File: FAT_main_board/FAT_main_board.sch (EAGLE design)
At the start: 4 parts, among them IC1 LM18200T, IC2 LM18200T, IC3 LM18200T

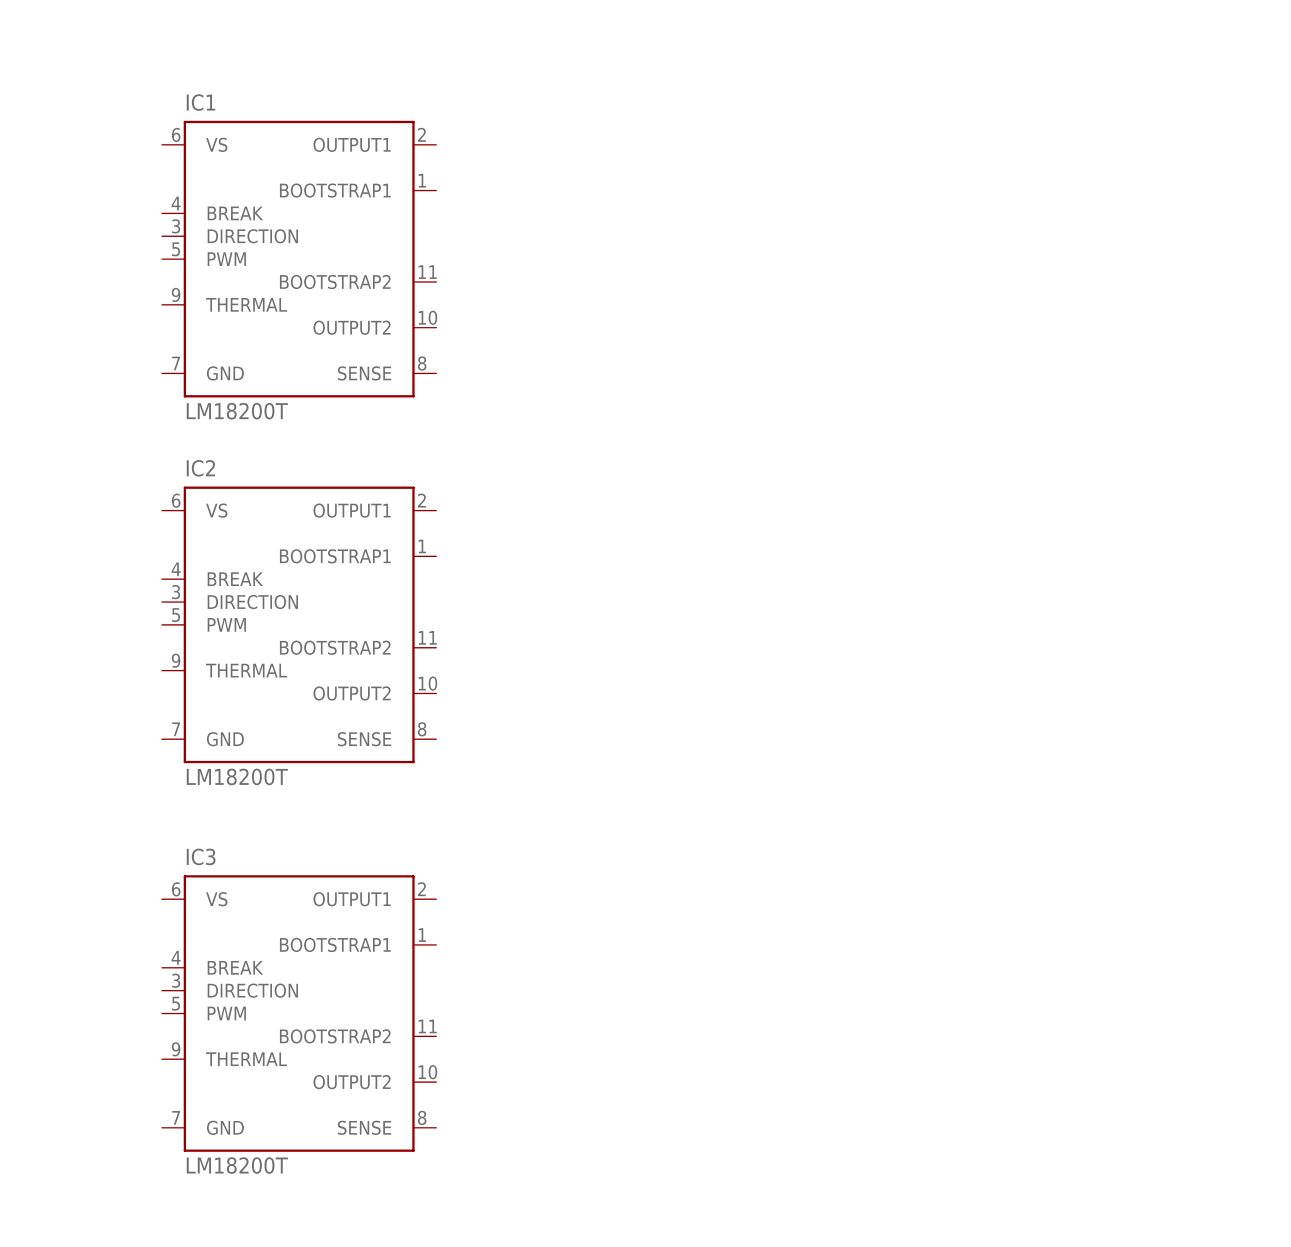
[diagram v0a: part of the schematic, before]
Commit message: [FAT board] Adds necessary components for H-bridges.
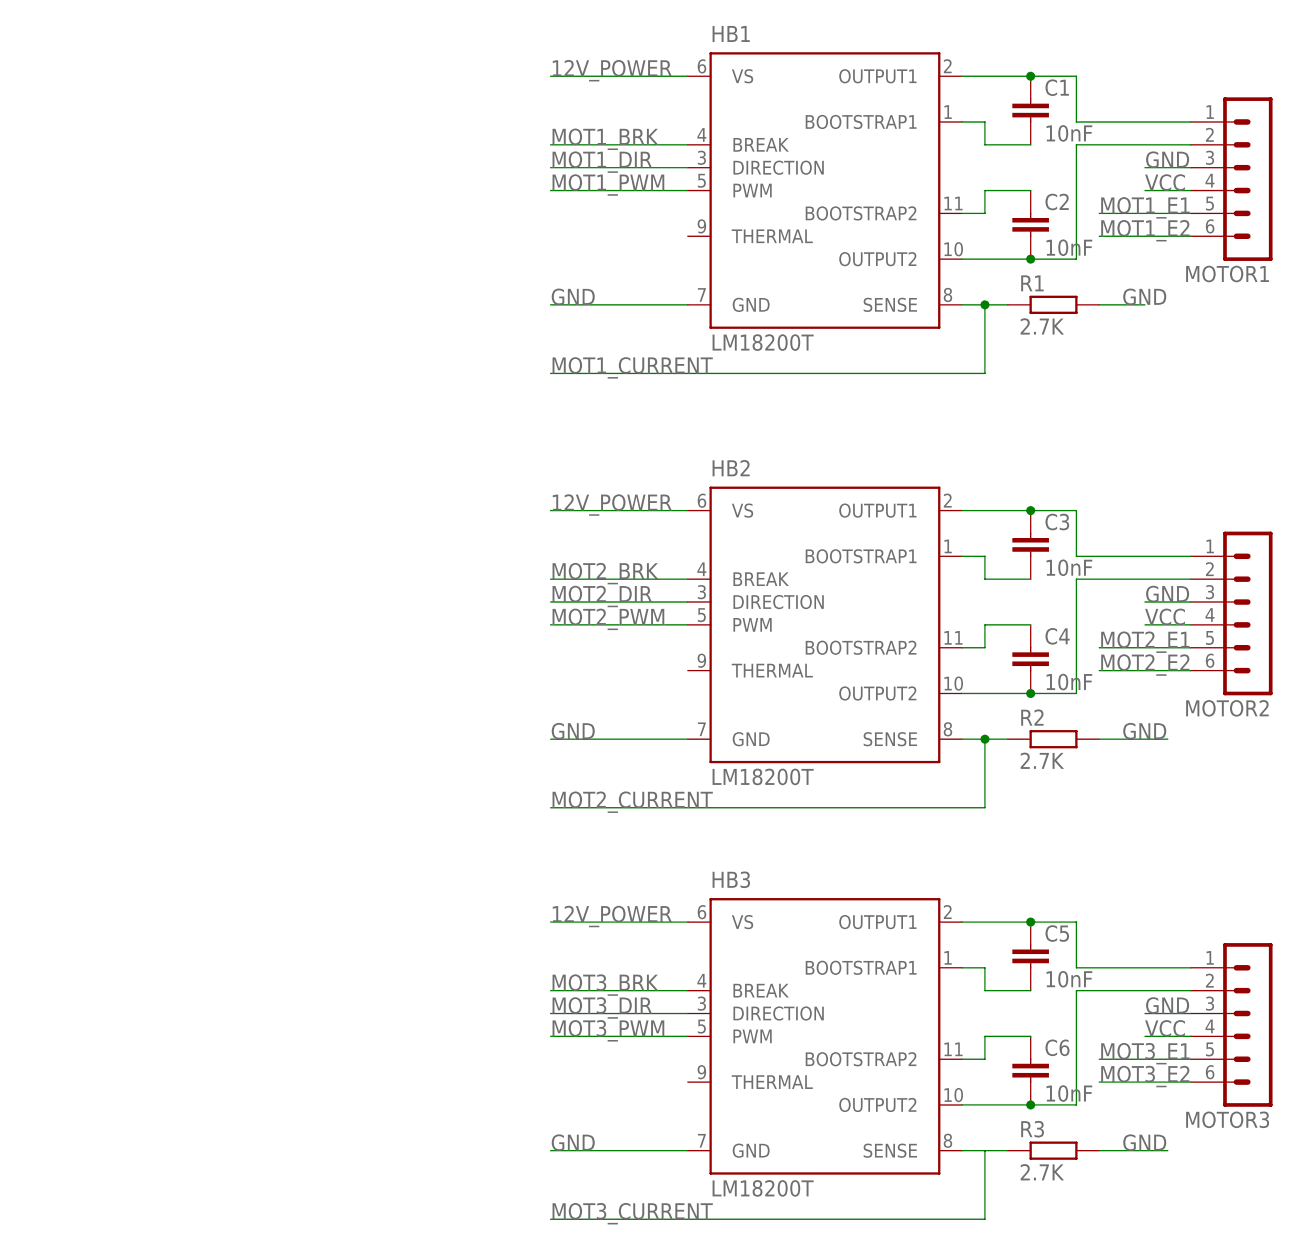
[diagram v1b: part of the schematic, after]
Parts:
- removed IC1, IC2, IC3: LM18200T, national-semiconductor:LM18200T
- added C1, C2, C3, C4, C5, C6: 10nF, resistor:C-EU050-035X075
- added HB1, HB2, HB3: LM18200T, national-semiconductor:LM18200T
- added MOTOR1, MOTOR2, MOTOR3: (no value), con-lstb:MA06-1
- added R1, R2, R3: 2.7K, resistor:R-EU_0204/7
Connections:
- new net 12V_POWER: HB1.VS, HB2.VS, HB3.VS
- new net GND: HB1.GND, HB2.GND, HB3.GND, MOTOR1.3, MOTOR2.3, MOTOR3.3, R1.2, R2.2, R3.2
- new net MOT1_BRK: HB1.BREAK
- new net MOT1_CURRENT: HB1.SENSE, R1.1
- new net MOT1_DIR: HB1.DIRECTION
- new net MOT1_E1: MOTOR1.5
- new net MOT1_E2: MOTOR1.6
- new net MOT1_PWM: HB1.PWM
- new net MOT2_BRK: HB2.BREAK
- new net MOT2_CURRENT: HB2.SENSE, R2.1
- new net MOT2_DIR: HB2.DIRECTION
- new net MOT2_E1: MOTOR2.5
- new net MOT2_E2: MOTOR2.6
- new net MOT2_PWM: HB2.PWM
- new net MOT3_BRK: HB3.BREAK
- new net MOT3_CURRENT: HB3.SENSE, R3.1
- new net MOT3_DIR: HB3.DIRECTION
- new net MOT3_E1: MOTOR3.5
- new net MOT3_E2: MOTOR3.6
- new net MOT3_PWM: HB3.PWM
- new net N$1: C1.1, HB1.OUTPUT1, MOTOR1.1
- new net N$14: C5.1, HB3.OUTPUT1, MOTOR3.1
- new net N$15: C5.2, HB3.BOOTSTRAP1
- new net N$16: C6.1, HB3.BOOTSTRAP2
- new net N$17: C6.2, HB3.OUTPUT2, MOTOR3.2
- new net N$2: C2.2, HB1.OUTPUT2, MOTOR1.2
- new net N$3: C1.2, HB1.BOOTSTRAP1
- new net N$4: C2.1, HB1.BOOTSTRAP2
- new net N$5: C3.1, HB2.OUTPUT1, MOTOR2.1
- new net N$6: C3.2, HB2.BOOTSTRAP1
- new net N$7: C4.1, HB2.BOOTSTRAP2
- new net N$8: C4.2, HB2.OUTPUT2, MOTOR2.2
- new net VCC: MOTOR1.4, MOTOR2.4, MOTOR3.4

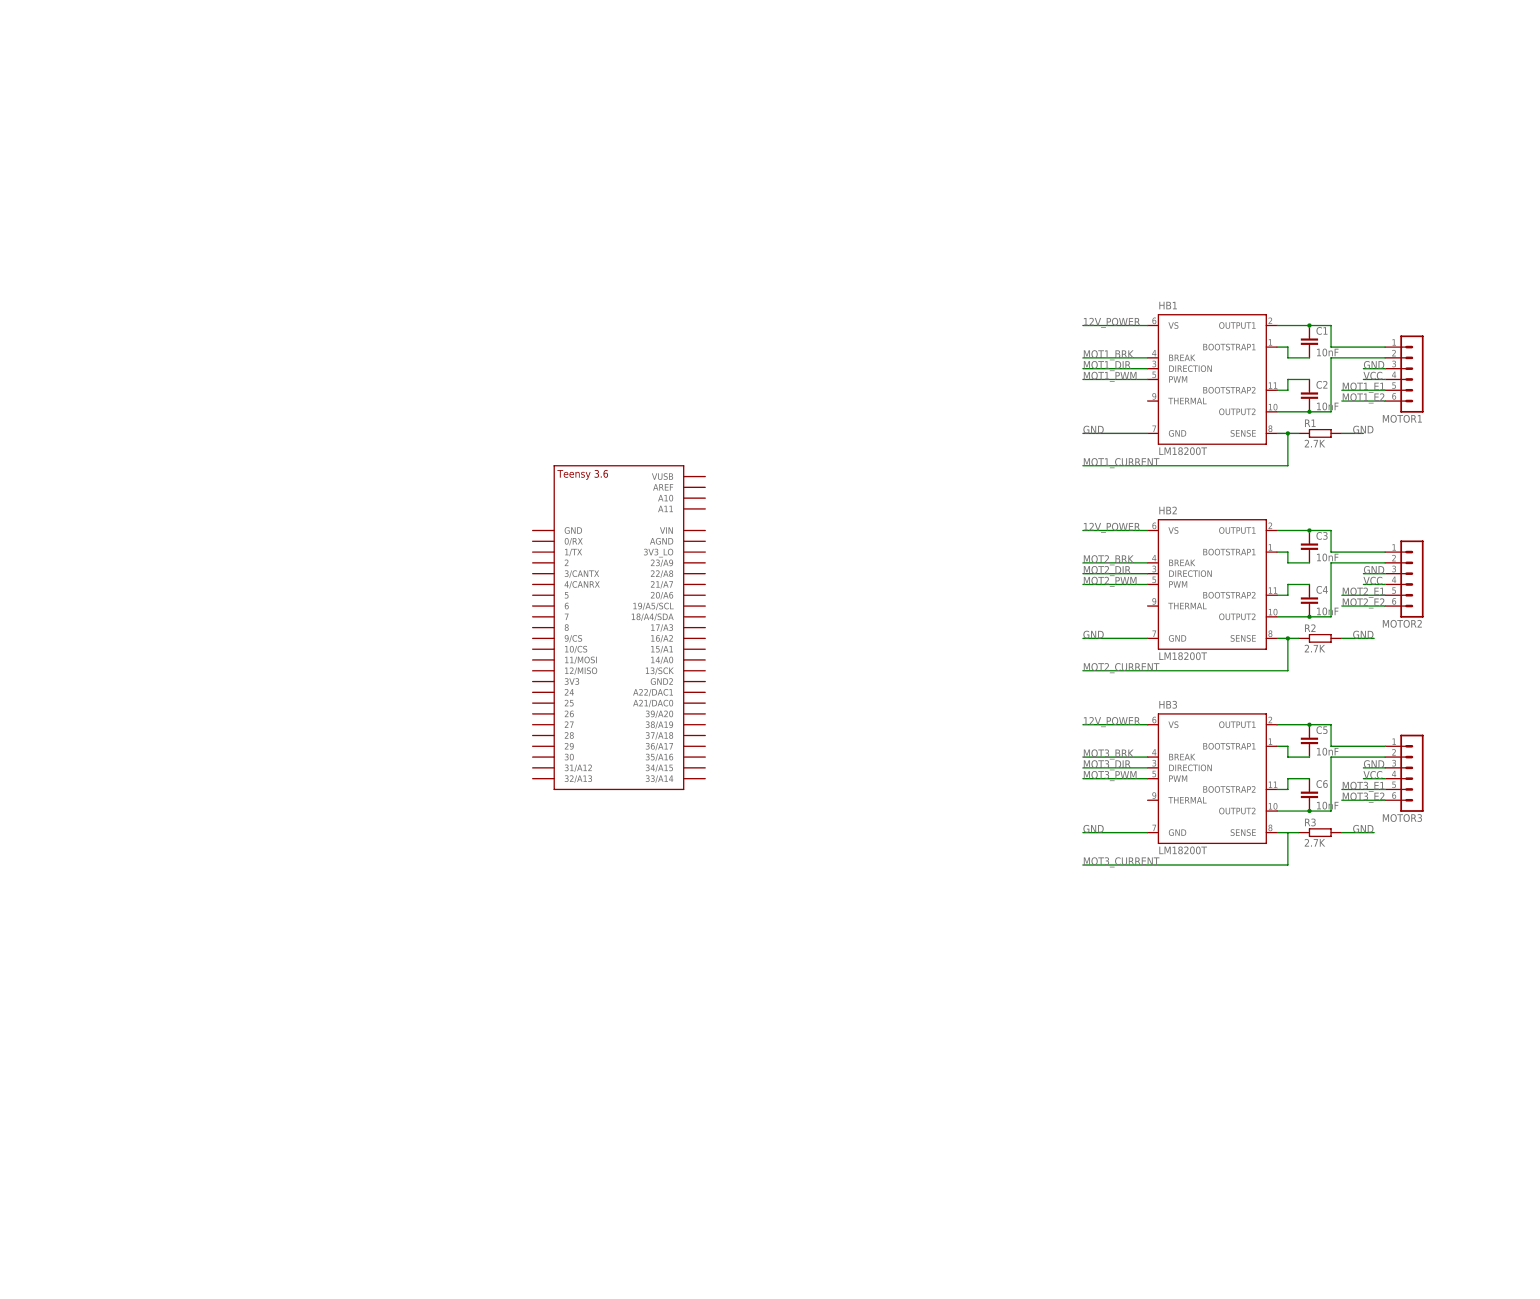
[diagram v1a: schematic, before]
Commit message: [FAT board] Connect motors to teensy and add dynamixel control.
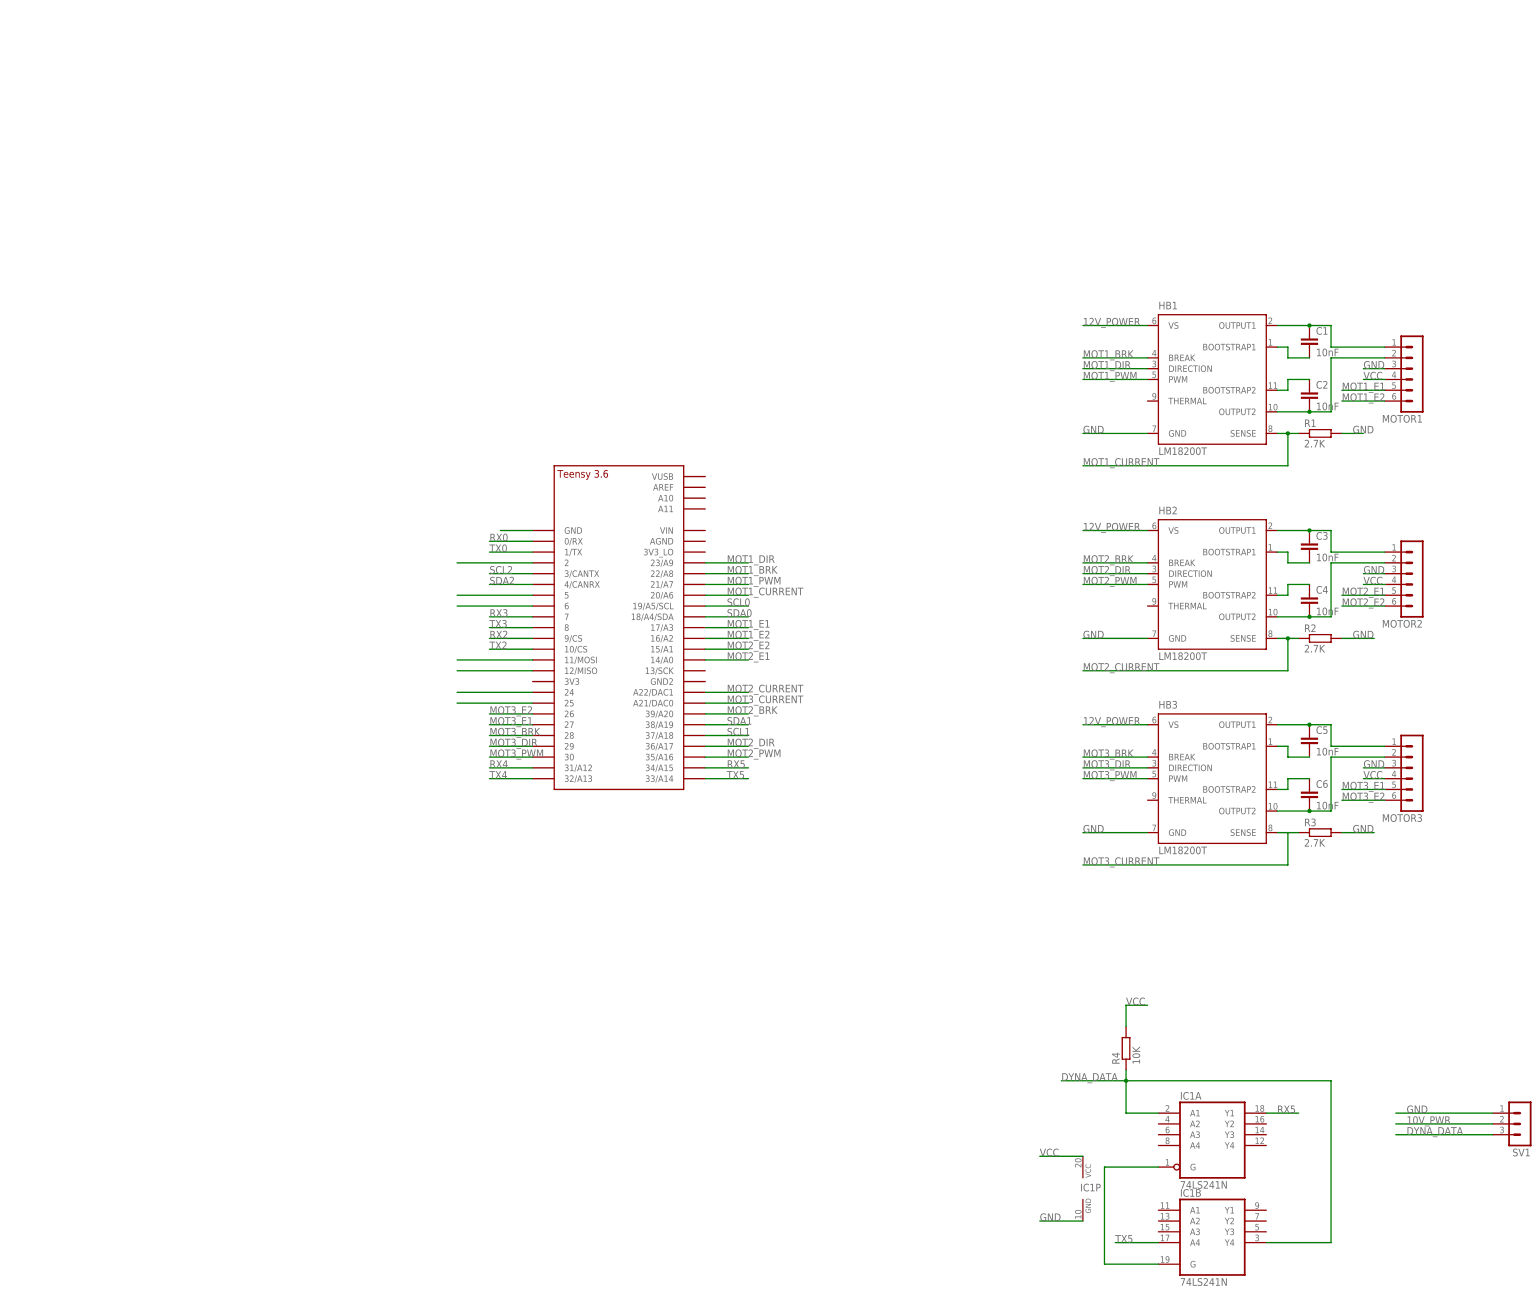
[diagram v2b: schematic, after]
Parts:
- added IC1: 74LS241N, 74xx-eu:74LS241N
- added R4: 10K, resistor:R-EU_0204/7
- added SV1: (no value), con-lstb:MA03-1
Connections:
- new net 10V_PWR: SV1.2
- new net DYNA_DATA: IC1A.A1, IC1B.Y4, R4.1, SV1.3
- new net N$10: U$1.6
- new net N$11: U$1.11/MOSI
- new net N$12: U$1.12/MISO
- new net N$13: U$1.GND
- new net N$18: U$1.2
- new net N$21: IC1A.G, IC1B.G
- new net N$40: U$1.25
- new net N$41: U$1.24
- new net N$9: U$1.5
- new net RX0: U$1.0/RX
- new net RX2: U$1.9/CS
- new net RX3: U$1.7
- new net RX4: U$1.31/A12
- new net RX5: IC1A.Y1, U$1.34/A15
- new net SCL0: U$1.19/A5/SCL
- new net SCL1: U$1.37/A18
- new net SCL2: U$1.3/CANTX
- new net SDA0: U$1.18/A4/SDA
- new net SDA1: U$1.38/A19
- new net SDA2: U$1.4/CANRX
- new net TX0: U$1.1/TX
- new net TX2: U$1.10/CS
- new net TX3: U$1.8
- new net TX4: U$1.32/A13
- new net TX5: IC1B.A4, U$1.33/A14
- net GND: now also IC1P.GND, SV1.1
- net MOT1_BRK: now also U$1.22/A8
- net MOT1_CURRENT: now also U$1.20/A6
- net MOT1_DIR: now also U$1.23/A9
- net MOT1_E1: now also U$1.17/A3
- net MOT1_E2: now also U$1.16/A2
- net MOT1_PWM: now also U$1.21/A7
- net MOT2_BRK: now also U$1.39/A20
- net MOT2_CURRENT: now also U$1.A22/DAC1
- net MOT2_DIR: now also U$1.36/A17
- net MOT2_E1: now also U$1.14/A0
- net MOT2_E2: now also U$1.15/A1
- net MOT2_PWM: now also U$1.35/A16
- net MOT3_BRK: now also U$1.28
- net MOT3_CURRENT: now also U$1.A21/DAC0
- net MOT3_DIR: now also U$1.29
- net MOT3_E1: now also U$1.27
- net MOT3_E2: now also U$1.26
- net MOT3_PWM: now also U$1.30
- net VCC: now also IC1P.VCC, R4.2
